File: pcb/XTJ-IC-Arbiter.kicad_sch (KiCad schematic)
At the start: 51 parts, among them J3 DTM13-12PA-R008, SW1 SW_DIP_x03, SW2 SW_DIP_x02, U1 LM2672N-5.0, U2 CDP68HC68S1, U3 Teensy4.0, U4 MCP2562-H-P, U5 TXB0104RGY

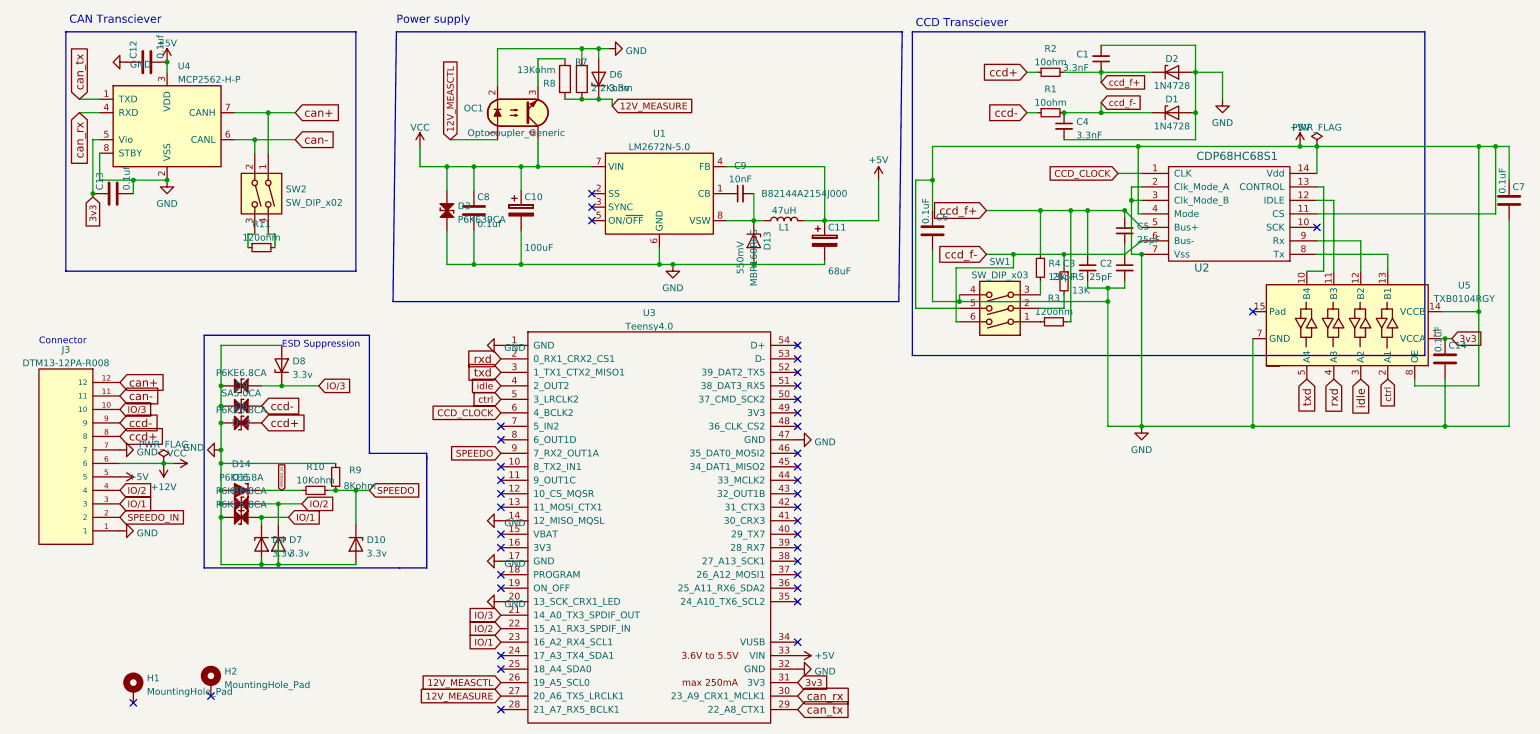
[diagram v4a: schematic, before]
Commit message: Tidy up even more vias
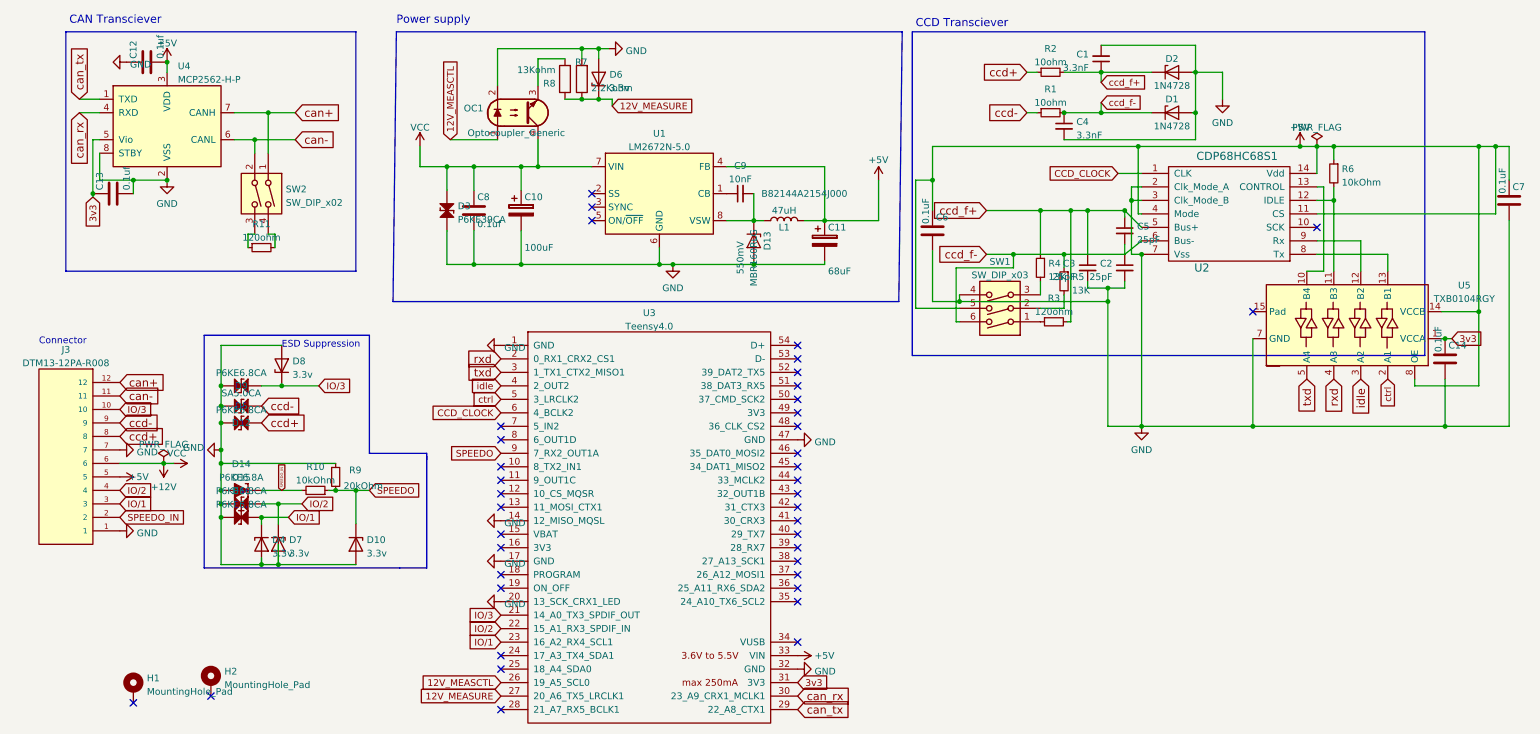
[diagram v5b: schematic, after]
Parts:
- added R6: 10kOhm, Resistor_THT:R_Axial_DIN0207_L6.3mm_D2.5mm_P7.62mm_Horizontal, symbol Device:R_Small
- R10: value 10Kohm -> 10kOhm
- R5: footprint Resistor_THT:R_Axial_DIN0207_L6.3mm_D2.5mm_P2.54mm_Vertical -> Resistor_THT:R_Axial_DIN0207_L6.3mm_D2.5mm_P7.62mm_Horizontal
- R9: value 8Kohm -> 20kOhm
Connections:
- net +5V: now also R6.1
- net at U2.12 (IDLE), U5.11 (B3): now also R6.2
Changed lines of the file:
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@@
   (junction (at 100.33 43.815) (diameter 0) (color 0 0 0 0)
   )
+  (junction (at 262.255 40.005) (diameter 0) (color 0 0 0 0)
+  )
   (junction (at 123.825 21.59) (diameter 0) (color 0 0 0 0)
   )
@@
   )
   (junction (at 52.705 92.075) (diameter 0) (color 0 0 0 0)
+  )
+  (junction (at 262.255 50.165) (diameter 0) (color 0 0 0 0)
   )
   (junction (at 112.395 43.815) (diameter 0) (color 0 0 0 0)
@@
     (stroke (width 0) (type default) (color 0 0 0 0))
   )
+  (wire (pts (xy 262.255 40.005) (xy 262.255 42.545))
+    (stroke (width 0) (type default) (color 0 0 0 0))
+  )
   (wire (pts (xy 60.325 118.745) (xy 63.5 118.745))
     (stroke (width 0) (type default) (color 0 0 0 0))
@@
     (stroke (width 0) (type default) (color 0 0 0 0))
   )
+  (wire (pts (xy 262.255 40.005) (xy 289.56 40.005))
+    (stroke (width 0) (type default) (color 0 0 0 0))
+  )
   (wire (pts (xy 59.055 38.735) (xy 59.055 41.275))
     (stroke (width 0) (type default) (color 0 0 0 0))
@@
     (stroke (width 0) (type default) (color 0 0 0 0))
   )
+  (wire (pts (xy 262.255 47.625) (xy 262.255 50.165))
+    (stroke (width 0) (type default) (color 0 0 0 0))
+  )
   (wire (pts (xy 211.455 26.035) (xy 218.44 26.035))
     (stroke (width 0) (type default) (color 0 0 0 0))
@@
     (stroke (width 0) (type default) (color 0 0 0 0))
   )
+  (polyline (pts (xy 80.645 97.79) (xy 80.645 75.565))
+    (stroke (width 0) (type default) (color 0 0 0 0))
+  )
+  (wire (pts (xy 90.17 43.815) (xy 95.25 43.815))
+    (stroke (width 0) (type default) (color 0 0 0 0))
+  )
+  (polyline (pts (xy 180.975 18.415) (xy 180.34 69.215))
+    (stroke (width 0) (type default) (color 0 0 0 0))
+  )
+  (wire (pts (xy 191.77 69.215) (xy 219.71 69.215))
+    (stroke (width 0) (type default) (color 0 0 0 0))
+  )
+  (polyline (pts (xy 91.44 113.03) (xy 91.44 119.38))
+    (stroke (width 0) (type default) (color 0 0 0 0))
+  )
+  (wire (pts (xy 52.705 109.855) (xy 52.705 118.745))
+    (stroke (width 0) (type default) (color 0 0 0 0))
+  )
+  (wire (pts (xy 137.795 62.23) (xy 153.035 62.23))
+    (stroke (width 0) (type default) (color 0 0 0 0))
+  )
+  (wire (pts (xy 63.5 114.935) (xy 63.5 118.745))
+    (stroke (width 0) (type default) (color 0 0 0 0))
+  )
+  (wire (pts (xy 73.025 104.775) (xy 74.295 104.775))
+    (stroke (width 0) (type default) (color 0 0 0 0))
+  )
   (wire (pts (xy 201.93 60.325) (xy 211.455 60.325))
     (stroke (width 0) (type default) (color 0 0 0 0))
   )
-  (polyline (pts (xy 80.645 97.79) (xy 80.645 75.565))
-    (stroke (width 0) (type default) (color 0 0 0 0))
-  )
-  (wire (pts (xy 90.17 43.815) (xy 95.25 43.815))
-    (stroke (width 0) (type default) (color 0 0 0 0))
-  )
-  (polyline (pts (xy 180.975 18.415) (xy 180.34 69.215))
-    (stroke (width 0) (type default) (color 0 0 0 0))
-  )
-  (wire (pts (xy 191.77 69.215) (xy 219.71 69.215))
-    (stroke (width 0) (type default) (color 0 0 0 0))
-  )
-  (polyline (pts (xy 91.44 113.03) (xy 91.44 119.38))
-    (stroke (width 0) (type default) (color 0 0 0 0))
-  )
-  (wire (pts (xy 52.705 109.855) (xy 52.705 118.745))
-    (stroke (width 0) (type default) (color 0 0 0 0))
-  )
-  (wire (pts (xy 137.795 62.23) (xy 153.035 62.23))
-    (stroke (width 0) (type default) (color 0 0 0 0))
-  )
-  (wire (pts (xy 63.5 114.935) (xy 63.5 118.745))
-    (stroke (width 0) (type default) (color 0 0 0 0))
-  )
-  (wire (pts (xy 73.025 104.775) (xy 74.295 104.775))
-    (stroke (width 0) (type default) (color 0 0 0 0))
-  )
   (wire (pts (xy 126.365 31.115) (xy 126.365 32.385))
     (stroke (width 0) (type default) (color 0 0 0 0))
@@
     (stroke (width 0) (type default) (color 0 0 0 0))
   )
-  (wire (pts (xy 259.08 40.005) (xy 289.56 40.005))
+  (wire (pts (xy 259.08 40.005) (xy 262.255 40.005))
     (stroke (width 0) (type default) (color 0 0 0 0))
   )
@@
       (effects (font (size 1.27 1.27)) (justify right))
     )
-    (property "Footprint" "Resistor_THT:R_Axial_DIN0207_L6.3mm_D2.5mm_P2.54mm_Vertical" (id 2) (at 211.455 65.405 0)
+    (property "Footprint" "Resistor_THT:R_Axial_DIN0207_L6.3mm_D2.5mm_P7.62mm_Horizontal" (id 2) (at 211.455 65.405 0)
       (effects (font (size 1.27 1.27)) hide)
     )
@@
       (effects (font (size 1.27 1.27)) (justify left))
     )
-    (property "Value" "8Kohm" (id 1) (at 75.7936 103.9372 0)
+    (property "Value" "20kOhm" (id 1) (at 75.7936 103.9372 0)
       (effects (font (size 1.27 1.27)) (justify left))
     )
@@
     (in_bom yes) (on_board yes) (fields_autoplaced)
     (property "Reference" "R10" (id 0) (at 70.485 100.3386 90))
-    (property "Value" "10Kohm" (id 1) (at 70.485 102.8755 90))
+    (property "Value" "10kOhm" (id 1) (at 70.485 102.8755 90))
     (property "Footprint" "Resistor_THT:R_Axial_DIN0204_L3.6mm_D1.6mm_P5.08mm_Horizontal" (id 2) (at 70.485 104.775 0)
       (effects (font (size 1.27 1.27)) hide)
@@
     (pin "2")
   )
+  (symbol (lib_id "Device:R_Small") (at 262.255 45.085 0) (mirror y) (unit 1)
+    (in_bom yes) (on_board yes) (fields_autoplaced)
+    (property "Reference" "R6" (id 0) (at 263.7536 44.2503 0)
+      (effects (font (size 1.27 1.27)) (justify right))
+    )
+    (property "Value" "10kOhm" (id 1) (at 263.7536 46.7872 0)
+      (effects (font (size 1.27 1.27)) (justify right))
+    )
+    (property "Footprint" "Resistor_THT:R_Axial_DIN0207_L6.3mm_D2.5mm_P7.62mm_Horizontal" (id 2) (at 262.255 45.085 0)
+      (effects (font (size 1.27 1.27)) hide)
+    )
+    (property "Datasheet" "~" (id 3) (at 262.255 45.085 0)
+      (effects (font (size 1.27 1.27)) hide)
+    )
+    (pin "1")
+    (pin "2")
+  )
   (symbol (lib_id "power:GND") (at 226.06 92.71 0) (unit 1)
     (in_bom yes) (on_board yes) (fields_autoplaced)
@@
     )
     (path "/06d873f9-980b-4b67-97c6-080c0e123b53"
-      (reference "R5") (unit 1) (value "13K") (footprint "Resistor_THT:R_Axial_DIN0207_L6.3mm_D2.5mm_P2.54mm_Vertical")
+      (reference "R5") (unit 1) (value "13K") (footprint "Resistor_THT:R_Axial_DIN0207_L6.3mm_D2.5mm_P7.62mm_Horizontal")
+    )
+    (path "/fb6a9717-bcbe-4a6e-a151-9ecd7f387ec6"
+      (reference "R6") (unit 1) (value "10kOhm") (footprint "Resistor_THT:R_Axial_DIN0207_L6.3mm_D2.5mm_P7.62mm_Horizontal")
     )
     (path "/46dfe61e-445b-4001-a194-0b00b8952b1c"
@@
     )
     (path "/9059ed6c-2e82-45a6-9f0b-5434ea9444db"
-      (reference "R9") (unit 1) (value "8Kohm") (footprint "Resistor_THT:R_Axial_DIN0204_L3.6mm_D1.6mm_P5.08mm_Horizontal")
+      (reference "R9") (unit 1) (value "20kOhm") (footprint "Resistor_THT:R_Axial_DIN0204_L3.6mm_D1.6mm_P5.08mm_Horizontal")
     )
     (path "/cac66376-f581-4dc6-bfeb-72131bd14457"
-      (reference "R10") (unit 1) (value "10Kohm") (footprint "Resistor_THT:R_Axial_DIN0204_L3.6mm_D1.6mm_P5.08mm_Horizontal")
+      (reference "R10") (unit 1) (value "10kOhm") (footprint "Resistor_THT:R_Axial_DIN0204_L3.6mm_D1.6mm_P5.08mm_Horizontal")
     )
     (path "/8d1ac031-3e67-4e7b-8e5c-6b675b8f2a5b"

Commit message: Design using the CDP transceiver but in TX only, neglecting idle etc
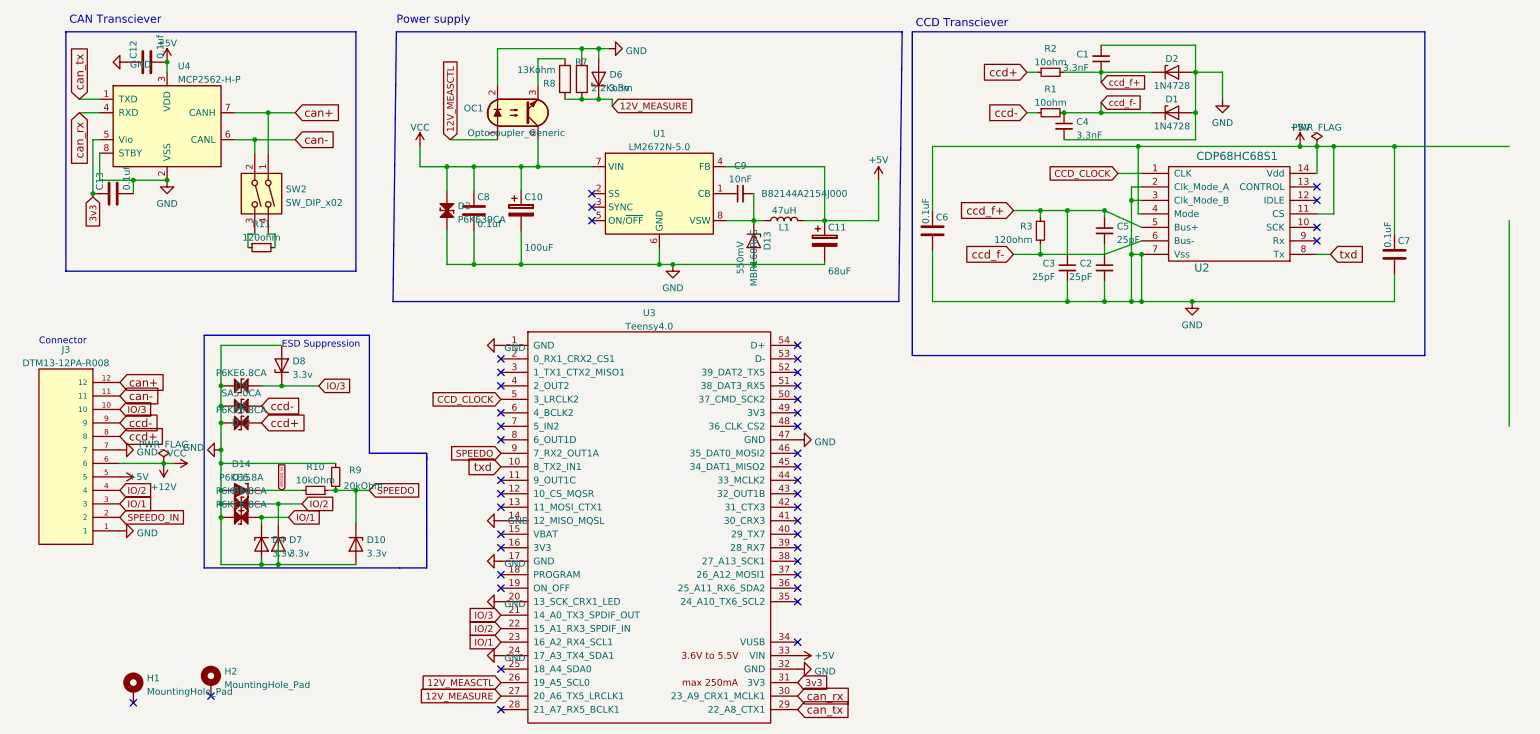
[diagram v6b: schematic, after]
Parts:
- removed C14: 0.1uF, Capacitor_THT:C_Disc_D3.8mm_W2.6mm_P2.50mm, symbol ccd_can_bridge-rescue:C
- removed R4, R5: 13K, Resistor_THT:R_Axial_DIN0207_L6.3mm_D2.5mm_P7.62mm_Horizontal, symbol Device:R_Small
- removed R6: 10kOhm, Resistor_THT:R_Axial_DIN0207_L6.3mm_D2.5mm_P7.62mm_Horizontal, symbol Device:R_Small
- removed SW1: SW_DIP_x03, Button_Switch_THT:SW_DIP_SPSTx03_Slide_9.78x9.8mm_W7.62mm_P2.54mm, symbol Switch:SW_DIP_x03
- removed U5: TXB0104RGY, Package_SO:SOIC-14_3.9x8.7mm_P1.27mm, symbol Logic_LevelTranslator:TXB0104RGY
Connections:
- net ctrl is gone; now on net CCD_CLOCK: U3.5 (3_LRCLK2)
- net CCD_CLOCK: no longer U3.6 (4_BCLK2)
- net GND: now also U3.24 (17_A3_TX4_SDA1)
- net ccd_f-: now also R3.1
- net txd: now also U2.8 (Tx), U3.10 (8_TX2_IN1); no longer U3.3 (1_TX1_CTX2_MISO1)
- net idle: no longer names the net of U3.4 (2_OUT2)
- net rxd: no longer names the net of U3.2 (0_RX1_CRX2_CS1)
- no-connect marks 40 -> 44
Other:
- moved on the sheet: C2, C3, C5, C7, R3

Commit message: Rearrange for tighter CCD signal traces
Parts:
- D1, D2: footprint Diode_THT:D_DO-41_SOD81_P7.62mm_Horizontal -> Diode_THT:D_DO-41_SOD81_P3.81mm_Vertical_KathodeUp
- R3: footprint Resistor_THT:R_Axial_DIN0207_L6.3mm_D2.5mm_P7.62mm_Horizontal -> Resistor_THT:R_Axial_DIN0207_L6.3mm_D2.5mm_P2.54mm_Vertical
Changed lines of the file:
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@@
     (property "Reference" "D1" (id 0) (at 231.775 31.115 0))
     (property "Value" "1N4728" (id 1) (at 231.775 36.195 0))
-    (property "Footprint" "Diode_THT:D_DO-41_SOD81_P7.62mm_Horizontal" (id 2) (at 231.775 33.655 0)
+    (property "Footprint" "Diode_THT:D_DO-41_SOD81_P3.81mm_Vertical_KathodeUp" (id 2) (at 231.775 33.655 0)
       (effects (font (size 1.27 1.27)) hide)
     )
@@
       (effects (font (size 1.27 1.27)) (justify right))
     )
-    (property "Footprint" "Resistor_THT:R_Axial_DIN0207_L6.3mm_D2.5mm_P7.62mm_Horizontal" (id 2) (at 207.01 55.88 0)
+    (property "Footprint" "Resistor_THT:R_Axial_DIN0207_L6.3mm_D2.5mm_P2.54mm_Vertical" (id 2) (at 207.01 55.88 0)
       (effects (font (size 1.27 1.27)) hide)
     )
@@
     (property "Reference" "D2" (id 0) (at 231.775 23.495 0))
     (property "Value" "1N4728" (id 1) (at 231.775 28.575 0))
-    (property "Footprint" "Diode_THT:D_DO-41_SOD81_P7.62mm_Horizontal" (id 2) (at 231.775 26.035 0)
+    (property "Footprint" "Diode_THT:D_DO-41_SOD81_P3.81mm_Vertical_KathodeUp" (id 2) (at 231.775 26.035 0)
       (effects (font (size 1.27 1.27)) hide)
     )
@@
     )
     (path "/1b315b47-8adf-49de-916b-225f0c5df700"
-      (reference "D1") (unit 1) (value "1N4728") (footprint "Diode_THT:D_DO-41_SOD81_P7.62mm_Horizontal")
+      (reference "D1") (unit 1) (value "1N4728") (footprint "Diode_THT:D_DO-41_SOD81_P3.81mm_Vertical_KathodeUp")
     )
     (path "/b2502fd8-e8a8-4cf0-b718-c349a466c0fa"
-      (reference "D2") (unit 1) (value "1N4728") (footprint "Diode_THT:D_DO-41_SOD81_P7.62mm_Horizontal")
+      (reference "D2") (unit 1) (value "1N4728") (footprint "Diode_THT:D_DO-41_SOD81_P3.81mm_Vertical_KathodeUp")
     )
     (path "/c9e7bce7-50cd-418b-ab12-64a1618f8b45"
@@
     )
     (path "/49ffc3f4-e717-41ef-9e7e-5cb511ac70a0"
-      (reference "R3") (unit 1) (value "120ohm") (footprint "Resistor_THT:R_Axial_DIN0207_L6.3mm_D2.5mm_P7.62mm_Horizontal")
+      (reference "R3") (unit 1) (value "120ohm") (footprint "Resistor_THT:R_Axial_DIN0207_L6.3mm_D2.5mm_P2.54mm_Vertical")
     )
     (path "/46dfe61e-445b-4001-a194-0b00b8952b1c"

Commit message: Tweak CCD routing just a bit more
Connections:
- net GND: now also U2.9 (Rx)
- no-connect marks 44 -> 43
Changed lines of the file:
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@@
   (junction (at 61.595 33.655) (diameter 0) (color 0 0 0 0)
+  )
+  (junction (at 259.08 69.215) (diameter 0) (color 0 0 0 0)
   )
   (no_connect (at 161.29 125.73))
@@
   (no_connect (at 161.29 80.01))
   (no_connect (at 161.29 77.47))
-  (no_connect (at 259.08 57.785))
   (no_connect (at 105.41 107.95))
   (no_connect (at 105.41 102.87))
@@
     (stroke (width 0) (type default) (color 0 0 0 0))
   )
-  (wire (pts (xy 235.585 69.215) (xy 273.685 69.215))
+  (wire (pts (xy 235.585 69.215) (xy 259.08 69.215))
     (stroke (width 0) (type default) (color 0 0 0 0))
   )
@@
     (stroke (width 0) (type default) (color 0 0 0 0))
   )
+  (wire (pts (xy 259.08 69.215) (xy 273.685 69.215))
+    (stroke (width 0) (type default) (color 0 0 0 0))
+  )
   (wire (pts (xy 295.275 53.975) (xy 295.275 92.71))
     (stroke (width 0) (type default) (color 0 0 0 0))
@@
     (stroke (width 0) (type default) (color 0 0 0 0))
   )
+  (wire (pts (xy 259.08 57.785) (xy 259.08 69.215))
+    (stroke (width 0) (type default) (color 0 0 0 0))
+  )
